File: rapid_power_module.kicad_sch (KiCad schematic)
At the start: 203 parts, among them J1 Conn_02x04_Top_Bottom, J10 JST-GH 4Pin, J11 SWD Header, J12 SWD Header, J16 USB_C_Receptacle_USB2.0, J17 TC2050, J2 Conn_02x03_Odd_Even, J3 Conn_02x04_Top_Bottom, J4 Conn_02x03_Odd_Even, J5 Molex MicroFit 2x2, J6 Molex MicroFit 2x2, J7 Molex MicroFit 2x2, J8 Molex MicroFit 2x2, Q1 AOSP21321, Q12 AOSP21321, Q2 AOSP21321, Q3 AOSP21321, Q4 HiDRV1, Q5 LoDRV1, Q6 HiDRV2, Q7 LoDRV2, SW1 KMR721NGLFS, SW2 KMR721NGLFS, U1 BQ25756RRVR, U10 L7805, U11 MCP2562-E-SN, U12 STM32F105RCTx, U13 AZ1117I-3.3, U14 TPD4E1U06, U15 TPD4E1U06, U2 CYPD3177-24LQ, U3 BQ76952PFBR, Y3 8MHz 12pF

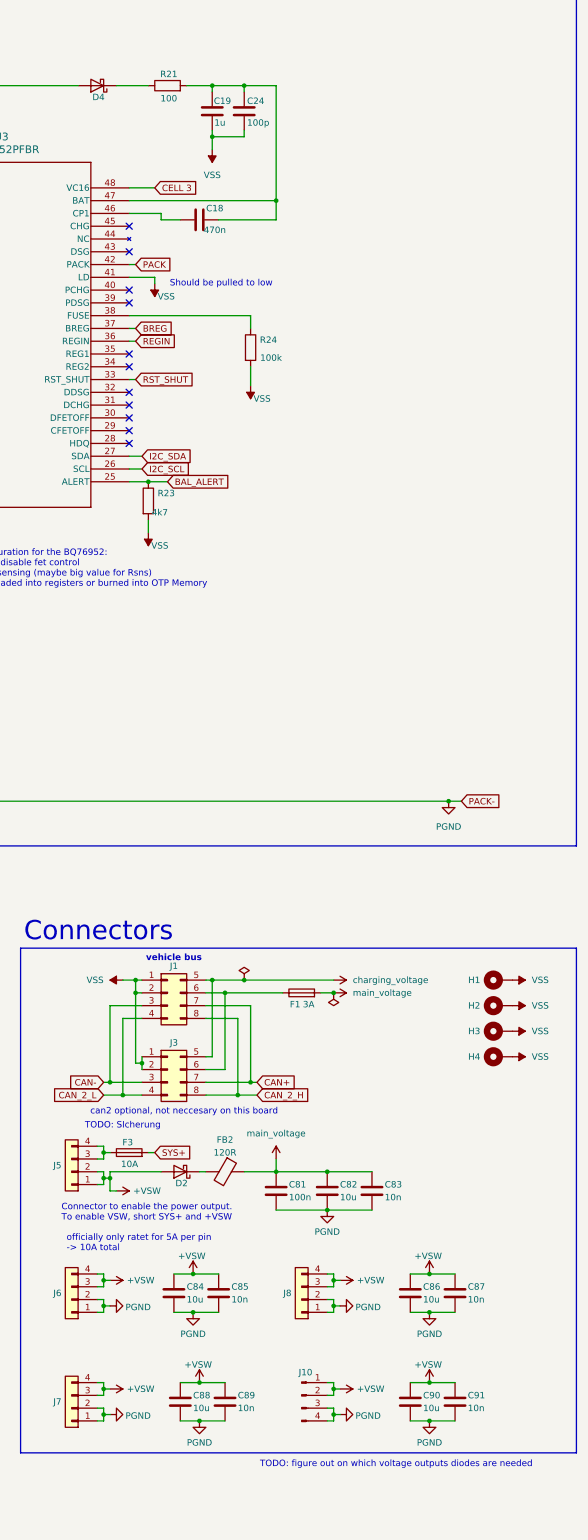
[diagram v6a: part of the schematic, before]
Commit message: fix diode and more routing work
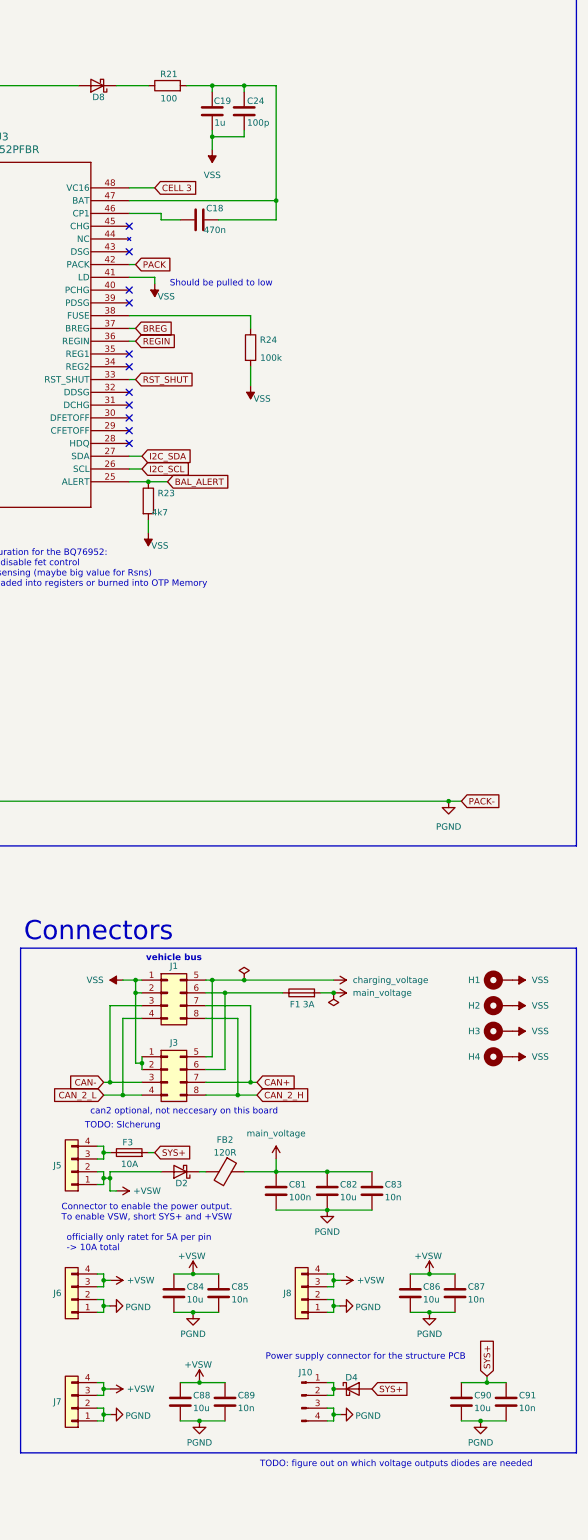
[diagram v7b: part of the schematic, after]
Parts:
- added D8: ~, Diode_SMD:ST_D_SMC, symbol Device:D_Schottky
- J11, J12: footprint Connector_PinHeader_2.54mm:PinHeader_1x04_P2.54mm_Vertical -> Connector_PinHeader_2.54mm:PinHeader_1x04_P2.54mm_Vertical_SMD_Pin1Left
- J2, J4: footprint Connector_PinHeader_2.54mm:PinHeader_2x03_P2.54mm_Vertical -> Connector_PinHeader_2.54mm:PinHeader_2x03_P2.54mm_Vertical_SMD
- R98: footprint Resistor_SMD:R_0603_1608Metric -> Resistor_SMD:R_0402_1005Metric
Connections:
- net +VSW: no longer C90.1, C91.1, J10.1 (Pin_1), J10.2 (Pin_2)
- net PACK+: now also C90.1, C91.1, D8.2 (A)
- net at R21.1: now also D8.1 (K); no longer D4.1 (K)
- new net: D4.1 (K), J10.1 (Pin_1), J10.2 (Pin_2)
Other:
- note added: "Power supply connector for the structure PCB"
- moved on the sheet: C90, C91, D4

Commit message: Added Pin connections from USB PD to STM, removed non essential resistors
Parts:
- removed R92, R93: 0R, Resistor_SMD:R_0402_1005Metric, symbol Device:R_Small
- added C20: 1u, Capacitor_SMD:C_0402_1005Metric, symbol Device:C_Small
- added R39: 4.7k, Resistor_SMD:R_0603_1608Metric, symbol Device:R_Small
- added R40, R42: 10k, Resistor_SMD:R_0603_1608Metric, symbol Device:R_Small
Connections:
- net +3.3V: now also R39.1, R40.1, R42.1
- net D0+: now also U14.4 (IO3)
- net D0-: now also U14.5 (IO4)
- net PGND: now also C20.2
- net FLIP: now reaches U12.26 (PB0)
- net FLIP: now also U2.10 (FLIP), R39.2
- net FAULT: now reaches U12.27 (PB1)
- net FAULT: now also U2.9 (FAULT), R40.2
- net GPIO_1: now reaches U12.28 (PB2)
- net GPIO_1: now also U2.8 (GPIO_1), R42.2
- net at U2.24 (VCCD): now also C20.1
- no-connect marks 38 -> 35
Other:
- note removed: "TODO"
- moved on the sheet: C10, Q1, Q3, R5, R9
